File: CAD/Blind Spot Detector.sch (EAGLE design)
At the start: 2 parts, among them IC1 TINY13V-10PU

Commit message: Readjusted Grid
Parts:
- IC1: value TINY13V-10PU -> TINY13-20PU; device atmel:TINY13V-10PU -> atmel:TINY13-20PU
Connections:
- new net +5V: IC1.VCC, U$1.VCC
- new net GND: IC1.GND, U$1.GND
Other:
- moved on the sheet: IC1
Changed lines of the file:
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@@
 </classes>
 <parts>
+<part name="IC1" library="atmel" deviceset="TINY13" device="PU" technology="-20"/>
 <part name="U$1" library="Ultrasonic_sensor" deviceset="ULTRASONIC_SENSOR" device=""/>
-<part name="IC1" library="atmel" deviceset="TINY13" device="PU" technology="V-10"/>
+<part name="P+1" library="supply1" deviceset="+5V" device=""/>
+<part name="P+2" library="supply1" deviceset="+5V" device=""/>
+<part name="GND1" library="supply1" deviceset="GND" device=""/>
+<part name="GND2" library="supply1" deviceset="GND" device=""/>
 </parts>
 <sheets>
@@
 </plain>
 <instances>
-<instance part="U$1" gate="G$1" x="125" y="42"/>
-<instance part="IC1" gate="G$1" x="58.54" y="43" rot="MR0"/>
+<instance part="IC1" gate="G$1" x="50.8" y="43.18" rot="MR0"/>
+<instance part="U$1" gate="G$1" x="116.84" y="40.64"/>
+<instance part="P+1" gate="1" x="78.74" y="66.04"/>
+<instance part="P+2" gate="1" x="119.38" y="68.58"/>
+<instance part="GND1" gate="1" x="119.38" y="22.86"/>
+<instance part="GND2" gate="1" x="78.74" y="30.48"/>
 </instances>
 <busses>
 </busses>
 <nets>
+<net name="GND" class="0">
+<segment>
+<pinref part="IC1" gate="G$1" pin="GND"/>
+<pinref part="GND2" gate="1" pin="GND"/>
+<wire x1="71.12" y1="38.1" x2="78.74" y2="38.1" width="0.1524" layer="91"/>
+<wire x1="78.74" y1="38.1" x2="78.74" y2="33.02" width="0.1524" layer="91"/>
+</segment>
+<segment>
+<pinref part="U$1" gate="G$1" pin="GND"/>
+<pinref part="GND1" gate="1" pin="GND"/>
+<wire x1="119.38" y1="27.94" x2="119.38" y2="25.4" width="0.1524" layer="91"/>
+</segment>
+</net>
+<net name="+5V" class="0">
+<segment>
+<pinref part="IC1" gate="G$1" pin="VCC"/>
+<wire x1="71.12" y1="55.88" x2="78.74" y2="55.88" width="0.1524" layer="91"/>
+<pinref part="P+1" gate="1" pin="+5V"/>
+<wire x1="78.74" y1="55.88" x2="78.74" y2="63.5" width="0.1524" layer="91"/>
+</segment>
+<segment>
+<pinref part="U$1" gate="G$1" pin="VCC"/>
+<pinref part="P+2" gate="1" pin="+5V"/>
+<wire x1="119.38" y1="63.5" x2="119.38" y2="66.04" width="0.1524" layer="91"/>
+</segment>
+</net>
 </nets>
 </sheet>

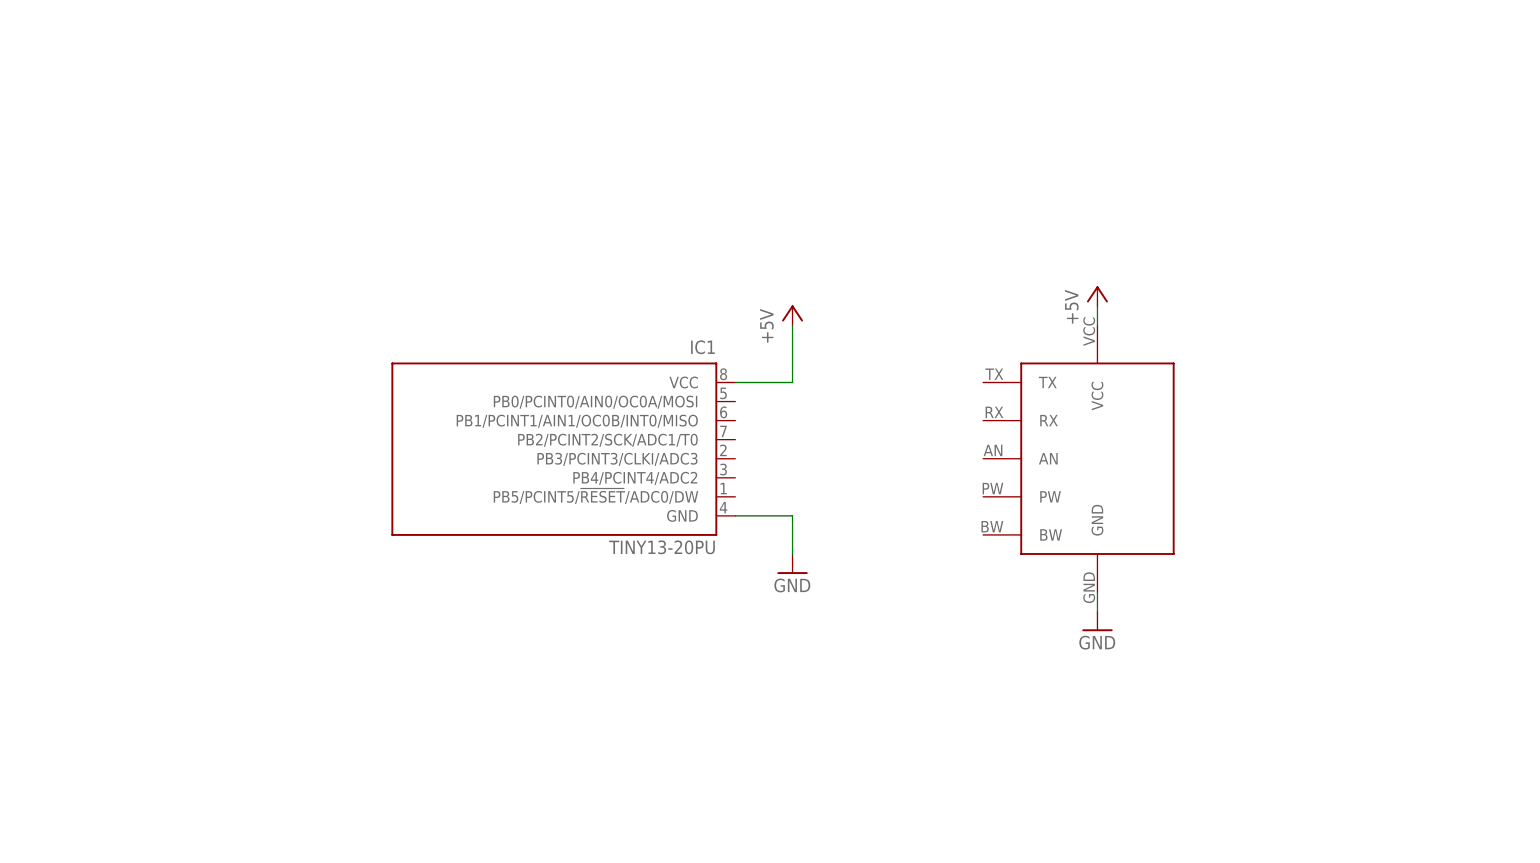
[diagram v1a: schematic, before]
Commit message: Voltage reg and supply
Power source, turn signal switch, linear voltage regulator and bypass
caps added to schematic
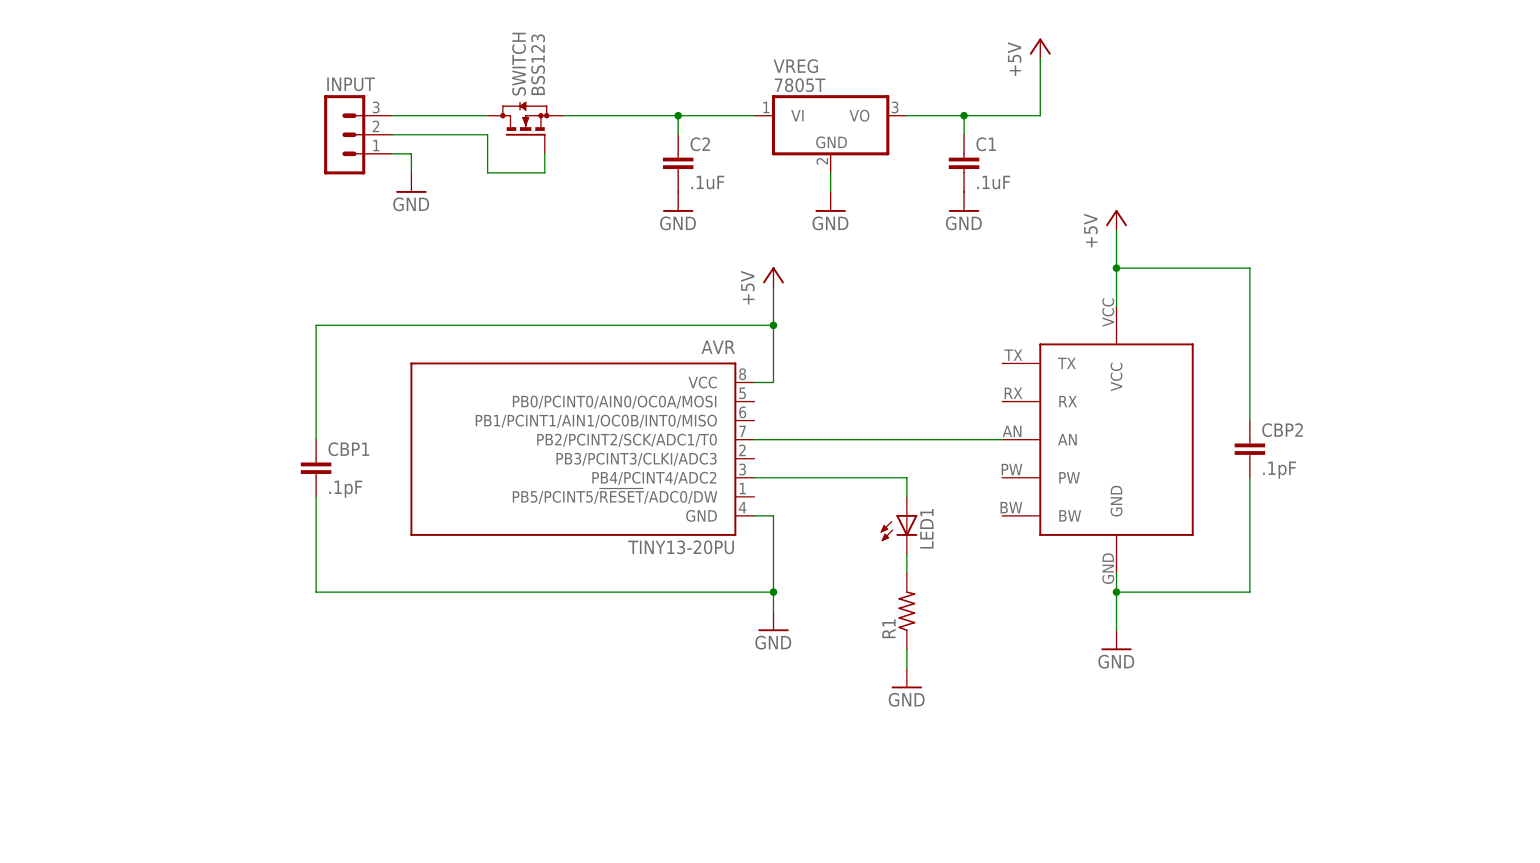
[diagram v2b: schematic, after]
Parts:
- removed IC1: TINY13-20PU, atmel:TINY13-20PU
- removed U$1: ULTRASONIC_SENSOR, Ultrasonic_sensor:ULTRASONIC_SENSOR
- added AVR: TINY13-20PU, atmel:TINY13-20PU
- added C1, C2: .1uF, rcl:C-EUC0805
- added CBP1, CBP2: .1pF, rcl:C-EUC0805
- added INPUT: (no value), con-lstb:MA03-1
- added LED1: (no value), led:LED5MM
- added R1: (no value), rcl:R-US_R0805
- added SWITCH: BSS123, transistor-small-signal:BSS123
- added ULTRA_SEN: ULTRASONIC_SENSOR, Ultrasonic_sensor:ULTRASONIC_SENSOR
- added VREG: 7805T, linear:7805T
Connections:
- new net BATTERY: INPUT.3, SWITCH.D
- new net N$1: C2.1, SWITCH.S, VREG.VI
- new net N$2: AVR.PB2/PCINT2/SCK/ADC1/T0, ULTRA_SEN.AN
- new net N$3: LED1.C, R1.2
- new net N$4: AVR.PB4/PCINT4/ADC2, LED1.A
- new net TSIG: INPUT.2, SWITCH.G
- net +5V: now also AVR.VCC, C1.1, CBP1.1, CBP2.1, ULTRA_SEN.VCC, VREG.VO; no longer IC1.VCC, U$1.VCC
- net GND: now also AVR.GND, C1.2, C2.2, CBP1.2, CBP2.2, INPUT.1, R1.1, ULTRA_SEN.GND, VREG.GND; no longer IC1.GND, U$1.GND
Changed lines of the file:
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@@
 <layer number="97" name="Info" color="7" fill="1" visible="yes" active="yes"/>
 <layer number="98" name="Guide" color="6" fill="1" visible="yes" active="yes"/>
+<layer number="99" name="SpiceOrder" color="5" fill="1" visible="yes" active="yes"/>
 </layers>
 <schematic xreflabel="%F%N/%S.%C%R" xrefpart="/%S.%C%R">
@@
 </classes>
 <parts>
-<part name="IC1" library="atmel" deviceset="TINY13" device="PU" technology="-20"/>
-<part name="U$1" library="Ultrasonic_sensor" deviceset="ULTRASONIC_SENSOR" device=""/>
+<part name="ULTRA_SEN" library="Ultrasonic_sensor" deviceset="ULTRASONIC_SENSOR" device=""/>
+<part name="AVR" library="atmel" deviceset="TINY13" device="PU" technology="-20"/>
 <part name="P+1" library="supply1" deviceset="+5V" device=""/>
 <part name="P+2" library="supply1" deviceset="+5V" device=""/>
 <part name="GND1" library="supply1" deviceset="GND" device=""/>
 <part name="GND2" library="supply1" deviceset="GND" device=""/>
+<part name="CBP1" library="rcl" deviceset="C-EU" device="C0805" value=".1pF"/>
+<part name="CBP2" library="rcl" deviceset="C-EU" device="C0805" value=".1pF"/>
+<part name="C1" library="rcl" deviceset="C-EU" device="C0805" value=".1uF"/>
+<part name="C2" library="rcl" deviceset="C-EU" device="C0805" value=".1uF"/>
+<part name="GND3" library="supply1" deviceset="GND" device=""/>
+<part name="GND4" library="supply1" deviceset="GND" device=""/>
+<part name="GND5" library="supply1" deviceset="GND" device=""/>
+<part name="P+3" library="supply1" deviceset="+5V" device=""/>
+<part name="R1" library="rcl" deviceset="R-US_" device="R0805"/>
+<part name="VREG" library="linear" deviceset="78*" device="T" technology="05"/>
+<part name="GND6" library="supply1" deviceset="GND" device=""/>
+<part name="SWITCH" library="transistor-small-signal" deviceset="BSS123" device=""/>
+<part name="LED1" library="led" deviceset="LED" device="5MM"/>
+<part name="INPUT" library="con-lstb" deviceset="MA03-1" device=""/>
+<part name="GND7" library="supply1" deviceset="GND" device=""/>
 </parts>
 <sheets>
@@
 </plain>
 <instances>
-<instance part="IC1" gate="G$1" x="50.8" y="43.18" rot="MR0"/>
-<instance part="U$1" gate="G$1" x="116.84" y="40.64"/>
-<instance part="P+1" gate="1" x="78.74" y="66.04"/>
-<instance part="P+2" gate="1" x="119.38" y="68.58"/>
-<instance part="GND1" gate="1" x="119.38" y="22.86"/>
-<instance part="GND2" gate="1" x="78.74" y="30.48"/>
+<instance part="ULTRA_SEN" gate="G$1" x="119.38" y="43.18"/>
+<instance part="AVR" gate="G$1" x="53.34" y="43.18" rot="MR0"/>
+<instance part="P+1" gate="1" x="121.92" y="78.74"/>
+<instance part="P+2" gate="1" x="76.2" y="71.12"/>
+<instance part="GND1" gate="1" x="76.2" y="22.86"/>
+<instance part="GND2" gate="1" x="121.92" y="20.32"/>
+<instance part="CBP1" gate="G$1" x="15.24" y="45.72"/>
+<instance part="CBP2" gate="G$1" x="139.7" y="48.26"/>
+<instance part="C1" gate="G$1" x="101.6" y="86.36"/>
+<instance part="C2" gate="G$1" x="63.5" y="86.36"/>
+<instance part="GND3" gate="1" x="63.5" y="78.74"/>
+<instance part="GND4" gate="1" x="101.6" y="78.74"/>
+<instance part="GND5" gate="1" x="83.82" y="78.74"/>
+<instance part="P+3" gate="1" x="111.76" y="101.6"/>
+<instance part="R1" gate="G$1" x="93.98" y="25.4" rot="R90"/>
+<instance part="VREG" gate="A1" x="83.82" y="91.44"/>
+<instance part="GND6" gate="1" x="93.98" y="15.24"/>
+<instance part="SWITCH" gate="G$1" x="43.18" y="91.44" rot="R90"/>
+<instance part="LED1" gate="G$1" x="93.98" y="38.1"/>
+<instance part="INPUT" gate="G$1" x="17.78" y="88.9"/>
+<instance part="GND7" gate="1" x="27.94" y="81.28"/>
 </instances>
 <busses>
 </busses>
 <nets>
+<net name="+5V" class="0">
+<segment>
+<pinref part="ULTRA_SEN" gate="G$1" pin="VCC"/>
+<wire x1="121.92" y1="66.04" x2="121.92" y2="71.12" width="0.1524" layer="91"/>
+<pinref part="P+1" gate="1" pin="+5V"/>
+<pinref part="CBP2" gate="G$1" pin="1"/>
+<wire x1="121.92" y1="71.12" x2="121.92" y2="76.2" width="0.1524" layer="91"/>
+<wire x1="121.92" y1="71.12" x2="139.7" y2="71.12" width="0.1524" layer="91"/>
+<wire x1="139.7" y1="71.12" x2="139.7" y2="50.8" width="0.1524" layer="91"/>
+<junction x="121.92" y="71.12"/>
+</segment>
+<segment>
+<pinref part="AVR" gate="G$1" pin="VCC"/>
+<wire x1="73.66" y1="55.88" x2="76.2" y2="55.88" width="0.1524" layer="91"/>
+<pinref part="P+2" gate="1" pin="+5V"/>
+<wire x1="76.2" y1="55.88" x2="76.2" y2="63.5" width="0.1524" layer="91"/>
+<pinref part="CBP1" gate="G$1" pin="1"/>
+<wire x1="76.2" y1="63.5" x2="76.2" y2="68.58" width="0.1524" layer="91"/>
+<wire x1="76.2" y1="63.5" x2="15.24" y2="63.5" width="0.1524" layer="91"/>
+<wire x1="15.24" y1="63.5" x2="15.24" y2="48.26" width="0.1524" layer="91"/>
+<junction x="76.2" y="63.5"/>
+</segment>
+<segment>
+<pinref part="P+3" gate="1" pin="+5V"/>
+<wire x1="111.76" y1="99.06" x2="111.76" y2="91.44" width="0.1524" layer="91"/>
+<pinref part="C1" gate="G$1" pin="1"/>
+<wire x1="93.98" y1="91.44" x2="101.6" y2="91.44" width="0.1524" layer="91"/>
+<wire x1="101.6" y1="91.44" x2="101.6" y2="88.9" width="0.1524" layer="91"/>
+<wire x1="111.76" y1="91.44" x2="101.6" y2="91.44" width="0.1524" layer="91"/>
+<junction x="101.6" y="91.44"/>
+<pinref part="VREG" gate="A1" pin="VO"/>
+</segment>
+</net>
 <net name="GND" class="0">
 <segment>
-<pinref part="IC1" gate="G$1" pin="GND"/>
 <pinref part="GND2" gate="1" pin="GND"/>
-<wire x1="71.12" y1="38.1" x2="78.74" y2="38.1" width="0.1524" layer="91"/>
-<wire x1="78.74" y1="38.1" x2="78.74" y2="33.02" width="0.1524" layer="91"/>
+<pinref part="ULTRA_SEN" gate="G$1" pin="GND"/>
+<wire x1="121.92" y1="30.48" x2="121.92" y2="27.94" width="0.1524" layer="91"/>
+<pinref part="CBP2" gate="G$1" pin="2"/>
+<wire x1="121.92" y1="27.94" x2="121.92" y2="22.86" width="0.1524" layer="91"/>
+<wire x1="139.7" y1="43.18" x2="139.7" y2="27.94" width="0.1524" layer="91"/>
+<wire x1="139.7" y1="27.94" x2="121.92" y2="27.94" width="0.1524" layer="91"/>
+<junction x="121.92" y="27.94"/>
 </segment>
 <segment>
-<pinref part="U$1" gate="G$1" pin="GND"/>
+<pinref part="AVR" gate="G$1" pin="GND"/>
+<wire x1="73.66" y1="38.1" x2="76.2" y2="38.1" width="0.1524" layer="91"/>
+<wire x1="76.2" y1="38.1" x2="76.2" y2="27.94" width="0.1524" layer="91"/>
 <pinref part="GND1" gate="1" pin="GND"/>
-<wire x1="119.38" y1="27.94" x2="119.38" y2="25.4" width="0.1524" layer="91"/>
+<pinref part="CBP1" gate="G$1" pin="2"/>
+<wire x1="76.2" y1="27.94" x2="76.2" y2="25.4" width="0.1524" layer="91"/>
+<wire x1="15.24" y1="40.64" x2="15.24" y2="27.94" width="0.1524" layer="91"/>
+<wire x1="15.24" y1="27.94" x2="76.2" y2="27.94" width="0.1524" layer="91"/>
+<junction x="76.2" y="27.94"/>
+</segment>
+<segment>
+<pinref part="C1" gate="G$1" pin="2"/>
+<pinref part="GND4" gate="1" pin="GND"/>
+</segment>
+<segment>
+<pinref part="C2" gate="G$1" pin="2"/>
+<pinref part="GND3" gate="1" pin="GND"/>
+</segment>
+<segment>
+<pinref part="GND5" gate="1" pin="GND"/>
+<wire x1="83.82" y1="81.28" x2="83.82" y2="83.82" width="0.1524" layer="91"/>
+<pinref part="VREG" gate="A1" pin="GND"/>
+</segment>
+<segment>
+<pinref part="R1" gate="G$1" pin="1"/>
+<pinref part="GND6" gate="1" pin="GND"/>
+<wire x1="93.98" y1="20.32" x2="93.98" y2="17.78" width="0.1524" layer="91"/>
+</segment>
+<segment>
+<pinref part="INPUT" gate="G$1" pin="1"/>
+<wire x1="25.4" y1="86.36" x2="27.94" y2="86.36" width="0.1524" layer="91"/>
+<wire x1="27.94" y1="86.36" x2="27.94" y2="83.82" width="0.1524" layer="91"/>
+<pinref part="GND7" gate="1" pin="GND"/>
 </segment>
 </net>
-<net name="+5V" class="0">
+<net name="N$1" class="0">
 <segment>
-<pinref part="IC1" gate="G$1" pin="VCC"/>
-<wire x1="71.12" y1="55.88" x2="78.74" y2="55.88" width="0.1524" layer="91"/>
-<pinref part="P+1" gate="1" pin="+5V"/>
-<wire x1="78.74" y1="55.88" x2="78.74" y2="63.5" width="0.1524" layer="91"/>
-</segment>
-<segment>
-<pinref part="U$1" gate="G$1" pin="VCC"/>
-<pinref part="P+2" gate="1" pin="+5V"/>
-<wire x1="119.38" y1="63.5" x2="119.38" y2="66.04" width="0.1524" layer="91"/>
+<pinref part="C2" gate="G$1" pin="1"/>
+<wire x1="63.5" y1="88.9" x2="63.5" y2="91.44" width="0.1524" layer="91"/>
+<wire x1="63.5" y1="91.44" x2="73.66" y2="91.44" width="0.1524" layer="91"/>
+<pinref part="VREG" gate="A1" pin="VI"/>
+<pinref part="SWITCH" gate="G$1" pin="S"/>
+<wire x1="48.26" y1="91.44" x2="63.5" y2="91.44" width="0.1524" layer="91"/>
+<junction x="63.5" y="91.44"/>
 </segment>
 </net>
+<net name="N$2" class="0">
+<segment>
+<pinref part="ULTRA_SEN" gate="G$1" pin="AN"/>
+<pinref part="AVR" gate="G$1" pin="PB2/PCINT2/SCK/ADC1/T0"/>
+<wire x1="106.68" y1="48.26" x2="73.66" y2="48.26" width="0.1524" layer="91"/>
+</segment>
+</net>
+<net name="N$4" class="0">
+<segment>
+<pinref part="AVR" gate="G$1" pin="PB4/PCINT4/ADC2"/>
+<wire x1="93.98" y1="43.18" x2="73.66" y2="43.18" width="0.1524" layer="91"/>
+<wire x1="93.98" y1="40.64" x2="93.98" y2="43.18" width="0.1524" layer="91"/>
+<pinref part="LED1" gate="G$1" pin="A"/>
+</segment>
+</net>
+<net name="TSIG" class="0">
+<segment>
+<pinref part="SWITCH" gate="G$1" pin="G"/>
+<wire x1="45.72" y1="86.36" x2="45.72" y2="83.82" width="0.1524" layer="91"/>
+<wire x1="38.1" y1="88.9" x2="38.1" y2="83.82" width="0.1524" layer="91"/>
+<wire x1="38.1" y1="83.82" x2="45.72" y2="83.82" width="0.1524" layer="91"/>
+<pinref part="INPUT" gate="G$1" pin="2"/>
+<wire x1="25.4" y1="88.9" x2="38.1" y2="88.9" width="0.1524" layer="91"/>
+</segment>
+</net>
+<net name="N$3" class="0">
+<segment>
+<pinref part="R1" gate="G$1" pin="2"/>
+<wire x1="93.98" y1="33.02" x2="93.98" y2="30.48" width="0.1524" layer="91"/>
+<pinref part="LED1" gate="G$1" pin="C"/>
+</segment>
+</net>
+<net name="BATTERY" class="0">
+<segment>
+<pinref part="INPUT" gate="G$1" pin="3"/>
+<pinref part="SWITCH" gate="G$1" pin="D"/>
+<wire x1="25.4" y1="91.44" x2="38.1" y2="91.44" width="0.1524" layer="91"/>
+</segment>
+</net>
